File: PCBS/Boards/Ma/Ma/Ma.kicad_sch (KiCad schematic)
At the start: 15 parts, among them J1 Conn_01x20_Socket, J2 Programmer, J3 PWM CHANNELS, J4 OLED SCREEN, SW1 SW_SPST, U1 ATmega328P-M, Y1 16MHz

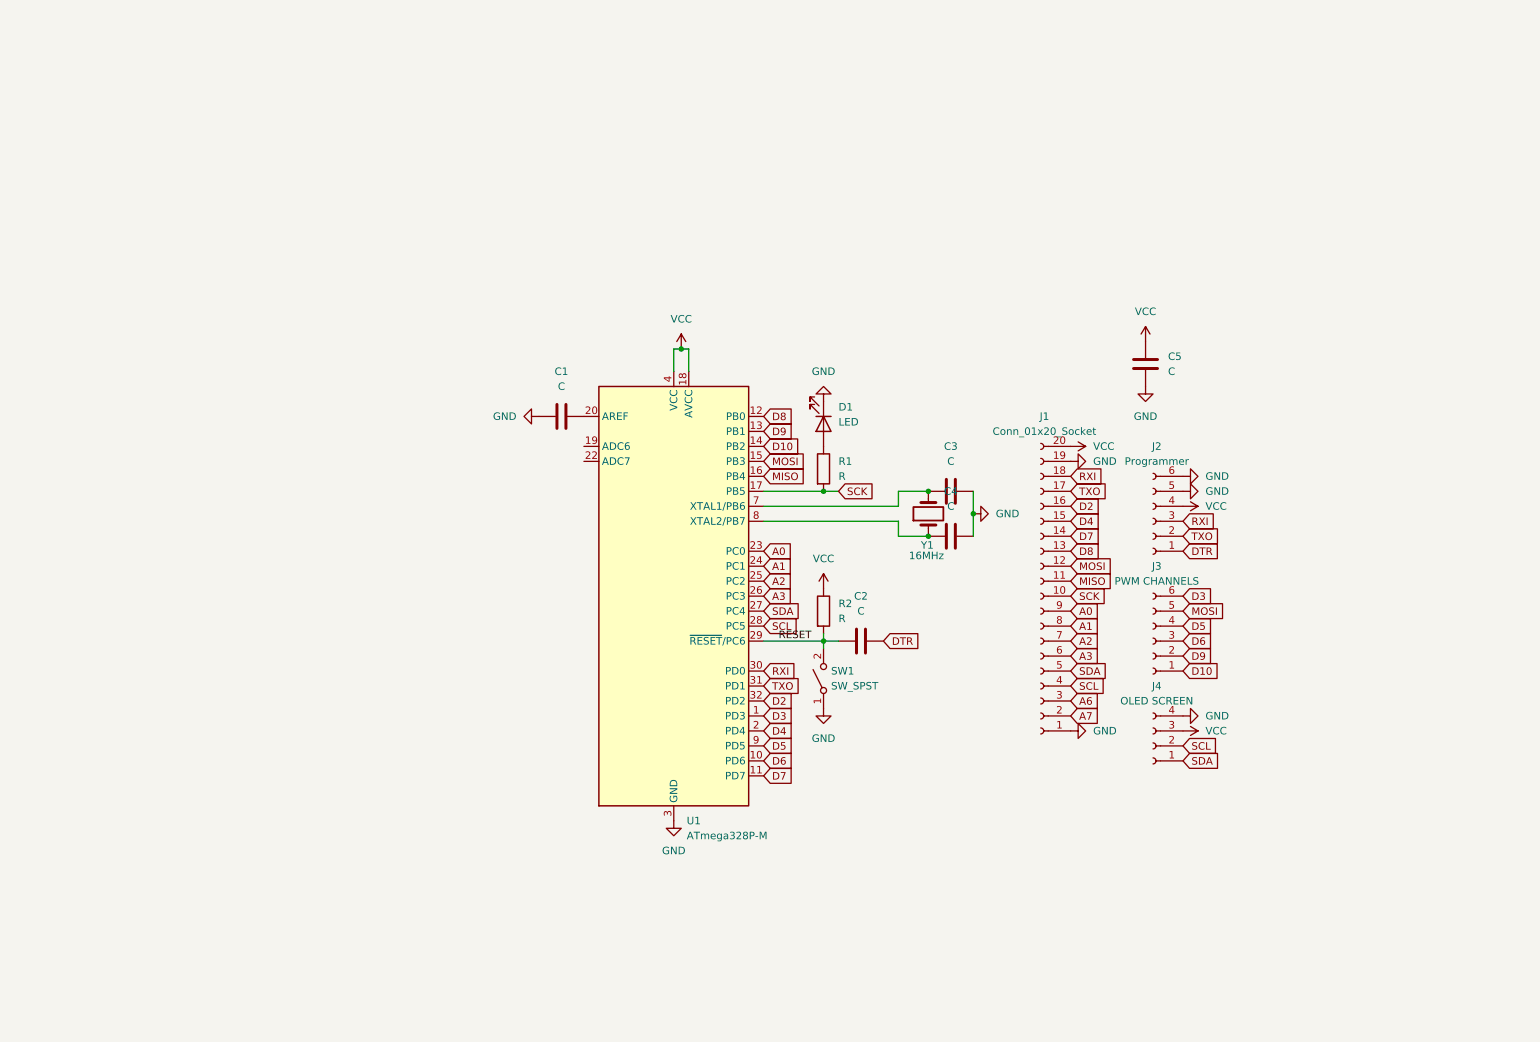
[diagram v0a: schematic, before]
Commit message: creates schematic and PCB for MA minisumo board
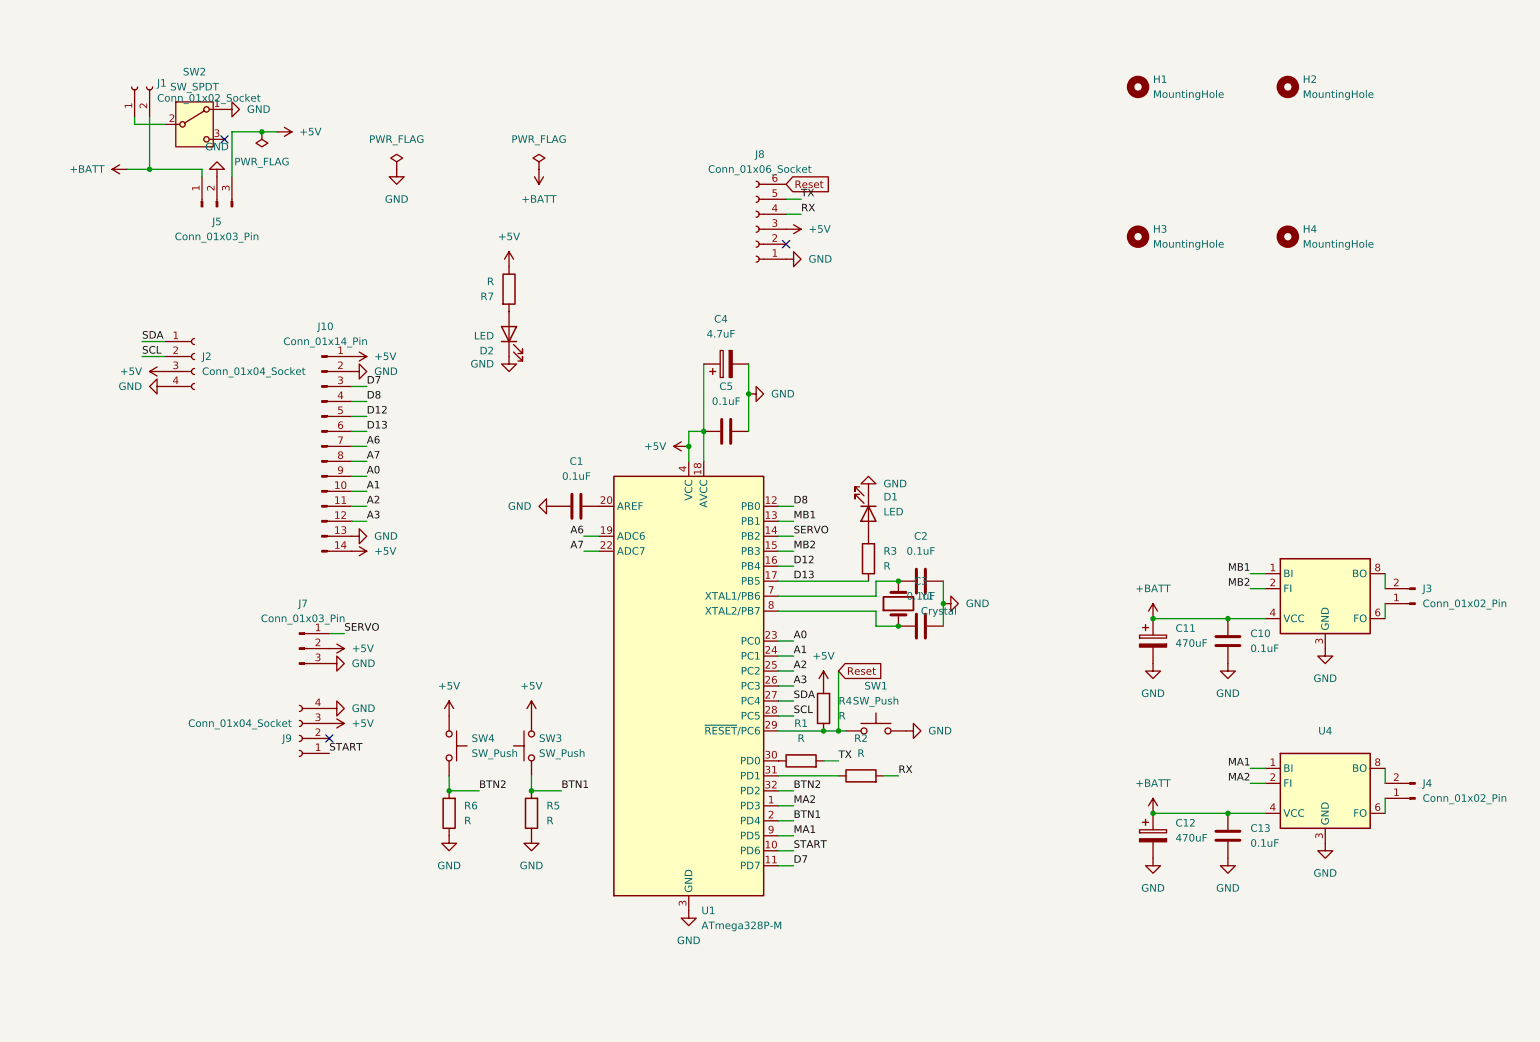
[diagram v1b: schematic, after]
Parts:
- removed C4: C, Capacitor_SMD:C_0805_2012Metric_Pad1.18x1.45mm_HandSolder, symbol Device:C
- removed J1: Conn_01x20_Socket, Connector_JST:JST_SH_SM20B-SRSS-TB_1x20-1MP_P1.00mm_Horizontal, symbol Connector:Conn_01x20_Socket
- removed J2: Programmer, Connector_PinSocket_2.54mm:PinSocket_1x06_P2.54mm_Vertical, symbol Connector:Conn_01x06_Socket
- removed J3: PWM CHANNELS, Connector_JST:JST_SH_SM06B-SRSS-TB_1x06-1MP_P1.00mm_Horizontal, symbol Connector:Conn_01x06_Socket
- removed J4: OLED SCREEN, Connector_PinSocket_2.54mm:PinSocket_1x04_P2.54mm_Vertical, symbol Connector:Conn_01x04_Socket
- removed SW1: SW_SPST, Button_Switch_SMD:SW_Push_1P1T_NO_CK_KMR2, symbol Switch:SW_SPST
- added C10, C13: 0.1uF, Capacitor_SMD:C_0805_2012Metric, symbol Device:C
- added C11, C12: 470uF, Capacitor_SMD:CP_Elec_8x10.5, symbol Device:C_Polarized
- added C4: 4.7uF, Capacitor_SMD:C_0805_2012Metric, symbol Device:C_Polarized
- added D2: LED, LED_SMD:LED_0603_1608Metric, symbol Device:LED
- added H1, H2, H3, H4: MountingHole, MountingHole:MountingHole_2.2mm_M2, symbol Mechanical:MountingHole
- added J1: Conn_01x02_Socket, Connector_AMASS:AMASS_XT30U-M_1x02_P5.0mm_Vertical, symbol Connector:Conn_01x02_Socket
- added J10: Conn_01x14_Pin, Connector_PinHeader_2.54mm:PinHeader_1x14_P2.54mm_Vertical, symbol Connector:Conn_01x14_Pin
- added J2, J9: Conn_01x04_Socket, Connector_PinSocket_2.54mm:PinSocket_1x04_P2.54mm_Vertical, symbol Connector:Conn_01x04_Socket
- added J3, J4: Conn_01x02_Pin, Connector_JST:JST_XH_B2B-XH-A_1x02_P2.50mm_Vertical, symbol Connector:Conn_01x02_Pin
- added J5: Conn_01x03_Pin, Package_TO_SOT_SMD:TO-252-2, symbol Connector:Conn_01x03_Pin
- added J7: Conn_01x03_Pin, EasyEDA:HDR-SMD_3P-P2.54-H-M-W13.3-N, symbol Connector:Conn_01x03_Pin
- added J8: Conn_01x06_Socket, EasyEDA:HDR-SMD_6P-P2.54-H-F-W11.7, symbol Connector:Conn_01x06_Socket
- added R3, R4, R5, R6, R7: R, Resistor_SMD:R_0603_1608Metric, symbol Device:R
- added SW1: SW_Push, Button_Switch_SMD:SW_Push_SPST_NO_Alps_SKRK, symbol Switch:SW_Push
- added SW2: SW_SPDT, EasyEDA:SW-TH_XKB_SS-12M11XX, symbol Switch:SW_SPDT
- added SW3, SW4: SW_Push, Button_Switch_SMD:SW_SPST_PTS810, symbol Switch:SW_Push
- added U3, U4: ~, Package_SO:SOP-8_3.9x4.9mm_P1.27mm, symbol Custom Development Boards:RZ7899_1
- C1, C2, C3, C5: value C -> 0.1uF; footprint Capacitor_SMD:C_0805_2012Metric_Pad1.18x1.45mm_HandSolder -> Capacitor_SMD:C_0805_2012Metric
- D1: footprint LED_SMD:LED_0805_2012Metric_Pad1.15x1.40mm_HandSolder -> LED_SMD:LED_0603_1608Metric
- R1, R2: footprint Resistor_SMD:R_0805_2012Metric_Pad1.20x1.40mm_HandSolder -> Resistor_SMD:R_0603_1608Metric
- Y1: value 16MHz -> Crystal; footprint Crystal:Crystal_SMD_3225-4Pin_3.2x2.5mm -> Crystal:Crystal_SMD_3215-2Pin_3.2x1.5mm
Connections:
- net DTR is gone; now on net GND: C2.2
- net A0: now also J10.9 (Pin_9)
- net A1: now also J10.10 (Pin_10)
- net A2: now also J10.11 (Pin_11)
- net A3: now also J10.12 (Pin_12)
- net A6: now also U1.19 (ADC6), J10.7 (Pin_7)
- net A7: now also U1.22 (ADC7), J10.8 (Pin_8)
- net D7: now also J10.3 (Pin_3)
- net D8: now also J10.4 (Pin_4)
- net GND: now also C10.2, C11.2, C12.2, C13.2, C4.2, D2.1 (K), J10.13 (Pin_13), J10.2 (Pin_2), J2.4 (Pin_4), J5.2 (Pin_2), J7.3 (Pin_3), J8.1 (Pin_1), J9.4 (Pin_4), R5.1, R6.1, SW1.2, SW2.1 (A), U3.3 (GND), U4.3 (GND)
- net SCL: now also J2.2 (Pin_2)
- net SDA: now also J2.1 (Pin_1)
- net at D1.2 (A): now also R3.2; no longer R1.1
- net at U1.7 (XTAL1/PB6), Y1.2: now also C2.1; no longer C3.1
- net at U1.8 (XTAL2/PB7), Y1.1: now also C3.1
- net D10 renamed SERVO
- net SERVO: now also J7.1 (Pin_1)
- net D2 renamed BTN2
- net BTN2: now also R6.2, SW4.2
- net D3 renamed MA2
- net MA2: now also U4.2 (FI)
- net D4 renamed BTN1
- net BTN1: now also R5.2, SW3.1
- net D5 renamed MA1
- net MA1: now also U4.1 (BI)
- net D6 renamed START
- net START: now also J9.1 (Pin_1)
- net D9 renamed MB1
- net MB1: now also U3.1 (BI)
- net MISO renamed D12
- net D12: now also J10.5 (Pin_5)
- net MOSI renamed MB2
- net MB2: now also U3.2 (FI)
- removed net RESET: C2.1, R2.2, U1.29 (~{RESET}/PC6)
- net RXI: no longer names the net of U1.30 (PD0)
- net RXI: now also R1.1
- net SCK renamed D13
- net D13: now also J10.6 (Pin_6), R3.1; no longer R1.2
- net TXO: no longer names the net of U1.31 (PD1)
- net TXO: now also R2.1
- net VCC renamed +5V
- net +5V: now also C4.1, J10.1 (Pin_1), J10.14 (Pin_14), J2.3 (Pin_3), J5.3 (Pin_3), J7.2 (Pin_2), J8.3 (Pin_3), J9.3 (Pin_3), R4.2, R7.1, SW3.2, SW4.1; no longer R2.1
- new net: D2.2 (A), R7.2
- new net: J1.1 (Pin_1), SW2.2 (B)
- new net: J4.1 (Pin_1), U4.5 (FO), U4.6 (FO)
- new net: J4.2 (Pin_2), U4.7 (BO), U4.8 (BO)
- new net: J3.1 (Pin_1), U3.5 (FO), U3.6 (FO)
- new net: J3.2 (Pin_2), U3.7 (BO), U3.8 (BO)
- new net +BATT: C10.1, C11.1, C12.1, C13.1, J1.2 (Pin_2), J5.1 (Pin_1), U3.4 (VCC), U4.4 (VCC)
- new net RX: J8.4 (Pin_4), R2.2
- new net Reset: J8.6 (Pin_6), R4.1, SW1.1, U1.29 (~{RESET}/PC6)
- new net TX: J8.5 (Pin_5), R1.2
- no-connect marks 0 -> 3

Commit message: updated readme and PCB files
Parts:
- removed J2, J9: Conn_01x04_Socket, Connector_PinSocket_2.54mm:PinSocket_1x04_P2.54mm_Vertical, symbol Connector:Conn_01x04_Socket
- removed J5: Conn_01x03_Pin, Package_TO_SOT_SMD:TO-252-2, symbol Connector:Conn_01x03_Pin
- removed U3, U4: ~, Package_SO:SOP-8_3.9x4.9mm_P1.27mm, symbol Custom Development Boards:RZ7899_1
- added C1, C3: C_Polarized, symbol Device:C_Polarized
- added C2: C, symbol Device:C
- added D1: D_Schottky, symbol Device:D_Schottky
- added J3, J6: Conn_01x04_Socket, symbol Connector:Conn_01x04_Socket
- added L1: L, symbol Device:L
- added Q1: PMOS, symbol Simulation_SPICE:PMOS
- added R1: R, symbol Device:R
- added U1: XL1509-5.0, Package_SO:SOIC-8_3.9x4.9mm_P1.27mm, symbol Regulator_Switching:XL1509-5.0
- added U3, U4: RZ7899-MS, EasyEDA:SOIC-8_L4.9-W3.9-P1.27-LS6.0-BL, symbol EasyEDA:RZ7899-MS
- renumbered C12 to C11, C13 to C12, C1 to C6, C2 to C7, C3 to C8, C11 to C9, D1 to D3, J8 to J2, J10 to J4, J7 to J5, J3 to J7, J4 to J8, R7 to R2, R2 to R5, R1 to R6, R6 to R7, R5 to R8, SW2 to SW1, SW1 to SW2, SW4 to SW3, SW3 to SW4, U1 to U2
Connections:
- net +5V: now also C3.1, J3.3 (Pin_3), J6.3 (Pin_3), L1.2, U1.3 (FB)
- net +BATT: now also Q1.3 (S), R1.2, U3.4 (VCC), U4.4 (VCC)
- net MA1: now also U4.1 (BI)
- net MA2: now also U4.2 (FI)
- net MB1: now also U3.1 (BI)
- net MB2: now also U3.2 (FI)
- net SCL: now also J3.2 (Pin_2)
- net SDA: now also J3.1 (Pin_1)
- net START: now also J6.1 (Pin_1)
- net TX: now also R6.1; no longer R6.2
- net -BATT: now reaches J1.1 (Pin_1), SW1.2 (B)
- net -BATT: now also C10.2, C11.2, C12.2, C4.2, C5.2, C6.1, C7.2, C8.2, C9.2, D2.1 (K), D3.1 (K), J2.1 (Pin_1), J4.13 (Pin_13), J4.2 (Pin_2), J5.3 (Pin_3), R7.1, R8.1, SW2.2, U2.21 (GND), U2.3 (GND), U2.33 (GND), U2.5 (GND), C1.2, C2.2, C3.2, D1.2 (A), J3.4 (Pin_4), J6.4 (Pin_4), U1.5 (GND), U1.6 (GND), U1.7 (GND), U1.8 (GND), U3.3 (GND), U4.3 (GND)
- net at SW1.3 (C): now also Q1.2 (G), R1.1
- net at J8.1 (Pin_1): now also U4.5 (FO), U4.6 (FO)
- net at J8.2 (Pin_2): now also U4.7 (BO), U4.8 (BO)
- net at U2.30 (PD0): now also R6.2; no longer R6.1
- net at J7.1 (Pin_1): now also U3.5 (FO), U3.6 (FO)
- net at J7.2 (Pin_2): now also U3.7 (BO), U3.8 (BO)
- removed net GND: C10.2, C11.2, C12.2, C4.2, C5.2, C6.1, C7.2, C8.2, C9.2, D2.1 (K), D3.1 (K), J2.1 (Pin_1), J4.13 (Pin_13), J4.2 (Pin_2), J5.3 (Pin_3), R7.1, R8.1, SW1.1 (A), SW2.2, U2.21 (GND), U2.3 (GND), U2.33 (GND), U2.5 (GND)
- net Reset renamed RESET
- new net: C1.1, C2.1, Q1.1 (D), U1.1 (VIN)
- new net: D1.1 (K), L1.1, U1.2 (OUT)
- no-connect marks 3 -> 4
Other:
- note added: "GPIO"
- note added: "I/O PINS"
- note added: "I2C"
- note added: "INPUT BUTTONS"
- note added: "MCU"
- note added: "MOTOR DRIVER UNIT"
- note added: "P Channel MOSFET High-Side Switch"
- note added: "PROGRAMMER"
- note added: "SERVO MODULE"
- note added: "START MODULE"
- note added: "VOLTAGE REGULATOR"
- company: (none) -> DENJU DIVISION
- title: (none) -> Ma AIO Board
- moved on the sheet: C10, C11, C12, C4, C5, C6, C7, C8, C9, D2, D3, H1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
